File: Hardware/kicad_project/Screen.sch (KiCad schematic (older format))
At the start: 9 parts

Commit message: update project with corrected schematic / pcb
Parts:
- C51, C52, C53, C54: renamed from C?; footprint RandomJunk:C_0603_nosilk -> Capacitors_SMD:C_0402_NoSilk; LCSC c19702 -> C52923
- C55, C56: renamed from C?; footprint RandomJunk:C_0603_nosilk -> Capacitors_SMD:C_0402_NoSilk; LCSC c19702 -> C15525
- LCD1: renamed from LCD?; footprint (none) -> RandomJunk:oled_ssd1306_14pin_91
- R14: renamed from R?; footprint (none) -> Resistors_SMD:R_0402_NoSilk; LCSC (none) -> C25744
- R15: renamed from R?; footprint (none) -> Resistors_SMD:R_0402_NoSilk; LCSC (none) -> C25778
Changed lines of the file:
@@
 sda
 $Comp
-L customLibrary:128x32OLED LCD?
+L customLibrary:128x32OLED LCD1
 U 1 1 6364F37E
 P 6500 3750
-F 0 "LCD?" H 6828 3796 50  0000 L CNN
+F 0 "LCD1" H 6828 3796 50  0000 L CNN
 F 1 "128x32OLED" H 6828 3705 50  0000 L CNN
-F 2 "" H 6550 3800 50  0001 C CNN
+F 2 "RandomJunk:oled_ssd1306_14pin_91" H 6550 3800 50  0001 C CNN
 F 3 "" H 6550 3800 50  0001 C CNN
 	1    6500 3750
@@
 $EndComp
 $Comp
-L Device:C C?
+L Device:C C51
 U 1 1 6364F385
 P 5750 3100
-F 0 "C?" H 5865 3146 50  0000 L CNN
+F 0 "C51" H 5865 3146 50  0000 L CNN
 F 1 "1u" H 5865 3055 50  0000 L CNN
-F 2 "RandomJunk:C_0603_nosilk" H 5788 2950 50  0001 C CNN
-F 3 "~" H 5750 3100 50  0001 C CNN
-F 4 "c19702" H 5750 3100 50  0001 C CNN "LCSC"
+F 2 "Capacitors_SMD:C_0402_NoSilk" H 5788 2950 50  0001 C CNN
+F 3 "" H 5750 3100 50  0001 C CNN
+F 4 "C52923" H 5750 3100 50  0001 C CNN "LCSC"
 	1    5750 3100
 	0    1    1    0
 $EndComp
 $Comp
-L Device:C C?
+L Device:C C52
 U 1 1 6364F38C
 P 5450 3300
-F 0 "C?" H 5565 3346 50  0000 L CNN
+F 0 "C52" H 5565 3346 50  0000 L CNN
 F 1 "1u" H 5565 3255 50  0000 L CNN
-F 2 "RandomJunk:C_0603_nosilk" H 5488 3150 50  0001 C CNN
+F 2 "Capacitors_SMD:C_0402_NoSilk" H 5488 3150 50  0001 C CNN
 F 3 "~" H 5450 3300 50  0001 C CNN
-F 4 "c19702" H 5450 3300 50  0001 C CNN "LCSC"
+F 4 "C52923" H 5450 3300 50  0001 C CNN "LCSC"
 	1    5450 3300
 	0    1    1    0
@@
 	5200 3400 6100 3400
 $Comp
-L Device:C C?
+L Device:C C53
 U 1 1 6364F39B
 P 4700 3500
-F 0 "C?" H 4815 3546 50  0000 L CNN
+F 0 "C53" H 4815 3546 50  0000 L CNN
 F 1 "1u" H 4815 3455 50  0000 L CNN
-F 2 "RandomJunk:C_0603_nosilk" H 4738 3350 50  0001 C CNN
+F 2 "Capacitors_SMD:C_0402_NoSilk" H 4738 3350 50  0001 C CNN
 F 3 "~" H 4700 3500 50  0001 C CNN
-F 4 "c19702" H 4700 3500 50  0001 C CNN "LCSC"
+F 4 "C52923" H 4700 3500 50  0001 C CNN "LCSC"
 	1    4700 3500
 	0    1    1    0
 $EndComp
 $Comp
-L Device:C C?
+L Device:C C54
 U 1 1 6364F3A2
 P 4700 3800
-F 0 "C?" H 4815 3846 50  0000 L CNN
+F 0 "C54" H 4815 3846 50  0000 L CNN
 F 1 "1u" H 4815 3755 50  0000 L CNN
-F 2 "RandomJunk:C_0603_nosilk" H 4738 3650 50  0001 C CNN
+F 2 "Capacitors_SMD:C_0402_NoSilk" H 4738 3650 50  0001 C CNN
 F 3 "~" H 4700 3800 50  0001 C CNN
-F 4 "c19702" H 4700 3800 50  0001 C CNN "LCSC"
+F 4 "C52923" H 4700 3800 50  0001 C CNN "LCSC"
 	1    4700 3800
 	0    1    1    0
 $EndComp
 $Comp
-L power:+3.3V #PWR?
+L power:+3.3V #PWR039
 U 1 1 6364F3A8
 P 4900 3300
-F 0 "#PWR?" H 4900 3150 50  0001 C CNN
+F 0 "#PWR039" H 4900 3150 50  0001 C CNN
 F 1 "+3.3V" H 4915 3473 50  0000 C CNN
 F 2 "" H 4900 3300 50  0001 C CNN
@@
 $EndComp
 $Comp
-L power:+3.3V #PWR?
+L power:+3.3V #PWR038
 U 1 1 6364F3AE
 P 5100 3100
-F 0 "#PWR?" H 5100 2950 50  0001 C CNN
+F 0 "#PWR038" H 5100 2950 50  0001 C CNN
 F 1 "+3.3V" H 5115 3273 50  0000 C CNN
 F 2 "" H 5100 3100 50  0001 C CNN
@@
 	5100 3800 6100 3800
 $Comp
-L power:GND #PWR?
+L power:GND #PWR040
 U 1 1 6364F3BB
 P 4450 4600
-F 0 "#PWR?" H 4450 4350 50  0001 C CNN
+F 0 "#PWR040" H 4450 4350 50  0001 C CNN
 F 1 "GND" V 4455 4472 50  0000 R CNN
 F 2 "" H 4450 4600 50  0001 C CNN
@@
 $EndComp
 $Comp
-L Device:C C?
+L Device:C C56
 U 1 1 6364F3C2
 P 4950 4400
-F 0 "C?" H 5065 4446 50  0000 L CNN
+F 0 "C56" H 5065 4446 50  0000 L CNN
 F 1 "10u" H 5065 4355 50  0000 L CNN
-F 2 "RandomJunk:C_0603_nosilk" H 4988 4250 50  0001 C CNN
+F 2 "Capacitors_SMD:C_0402_NoSilk" H 4988 4250 50  0001 C CNN
 F 3 "~" H 4950 4400 50  0001 C CNN
-F 4 "c19702" H 4950 4400 50  0001 C CNN "LCSC"
+F 4 "C15525" H 4950 4400 50  0001 C CNN "LCSC"
 	1    4950 4400
 	0    1    1    0
 $EndComp
 $Comp
-L Device:C C?
+L Device:C C55
 U 1 1 6364F3C9
 P 5400 4300
-F 0 "C?" H 5515 4346 50  0000 L CNN
+F 0 "C55" H 5515 4346 50  0000 L CNN
 F 1 "10u" H 5515 4255 50  0000 L CNN
-F 2 "RandomJunk:C_0603_nosilk" H 5438 4150 50  0001 C CNN
+F 2 "Capacitors_SMD:C_0402_NoSilk" H 5438 4150 50  0001 C CNN
 F 3 "~" H 5400 4300 50  0001 C CNN
-F 4 "c19702" H 5400 4300 50  0001 C CNN "LCSC"
+F 4 "C15525" H 5400 4300 50  0001 C CNN "LCSC"
 	1    5400 4300
 	0    1    1    0
 $EndComp
 $Comp
-L Device:R R?
+L Device:R R15
 U 1 1 6364F3CF
 P 5750 4200
-F 0 "R?" V 5543 4200 50  0000 C CNN
+F 0 "R15" V 5543 4200 50  0000 C CNN
 F 1 "330k" V 5634 4200 50  0000 C CNN
-F 2 "" V 5680 4200 50  0001 C CNN
+F 2 "Resistors_SMD:R_0402_NoSilk" V 5680 4200 50  0001 C CNN
 F 3 "~" H 5750 4200 50  0001 C CNN
+F 4 "C25778" H 5750 4200 50  0001 C CNN "LCSC"
 	1    5750 4200
 	0    1    1    0
@@
 	4450 3700 4450 3800
 $Comp
-L Device:R R?
+L Device:R R14
 U 1 1 6364F3E9
 P 5450 3900
-F 0 "R?" V 5243 3900 50  0000 C CNN
+F 0 "R14" V 5243 3900 50  0000 C CNN
 F 1 "10k" V 5334 3900 50  0000 C CNN
-F 2 "" V 5380 3900 50  0001 C CNN
+F 2 "Resistors_SMD:R_0402_NoSilk" V 5380 3900 50  0001 C CNN
 F 3 "~" H 5450 3900 50  0001 C CNN
+F 4 "C25744" H 5450 3900 50  0001 C CNN "LCSC"
 	1    5450 3900
 	0    1    1    0

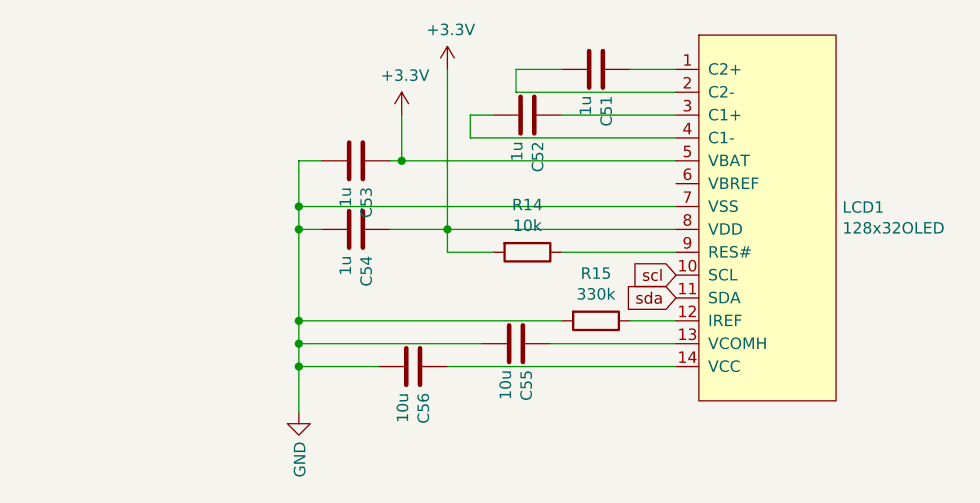
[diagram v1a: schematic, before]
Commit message: new hardware rev
- soft / latching power switch
- corrected mic
- added pullup to flash ss
- front & back enclosure plates
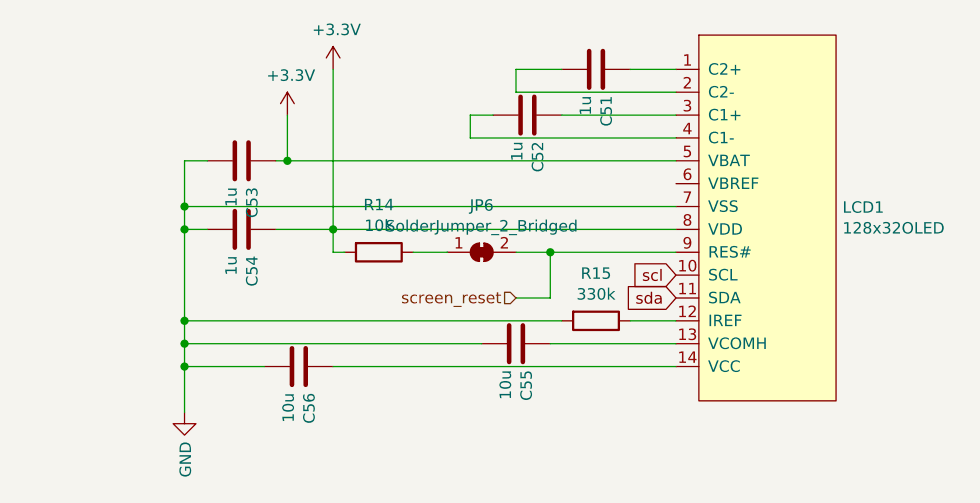
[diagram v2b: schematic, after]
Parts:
- added JP6: SolderJumper_2_Bridged, Jumper:SolderJumper-2_P1.3mm_Bridged_RoundedPad1.0x1.5mm, symbol Jumper:SolderJumper_2_Bridged
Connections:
- net at R14.1: now also JP6.1 (A); no longer LCD1.9 (RES#)
- new net screen_reset: JP6.2 (B), LCD1.9 (RES#)
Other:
- moved on the sheet: C53, C54, C56, R14
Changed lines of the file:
@@
 L Device:C C53
 U 1 1 6364F39B
-P 4700 3500
-F 0 "C53" H 4815 3546 50  0000 L CNN
-F 1 "1u" H 4815 3455 50  0000 L CNN
-F 2 "Capacitors_SMD:C_0402_NoSilk" H 4738 3350 50  0001 C CNN
-F 3 "~" H 4700 3500 50  0001 C CNN
-F 4 "C52923" H 4700 3500 50  0001 C CNN "LCSC"
-	1    4700 3500
+P 4200 3500
+F 0 "C53" H 4315 3546 50  0000 L CNN
+F 1 "1u" H 4315 3455 50  0000 L CNN
+F 2 "Capacitors_SMD:C_0402_NoSilk" H 4238 3350 50  0001 C CNN
+F 3 "~" H 4200 3500 50  0001 C CNN
+F 4 "C52923" H 4200 3500 50  0001 C CNN "LCSC"
+	1    4200 3500
 	0    1    1    0
 $EndComp
@@
 L Device:C C54
 U 1 1 6364F3A2
-P 4700 3800
-F 0 "C54" H 4815 3846 50  0000 L CNN
-F 1 "1u" H 4815 3755 50  0000 L CNN
-F 2 "Capacitors_SMD:C_0402_NoSilk" H 4738 3650 50  0001 C CNN
-F 3 "~" H 4700 3800 50  0001 C CNN
-F 4 "C52923" H 4700 3800 50  0001 C CNN "LCSC"
-	1    4700 3800
+P 4200 3800
+F 0 "C54" H 4315 3846 50  0000 L CNN
+F 1 "1u" H 4315 3755 50  0000 L CNN
+F 2 "Capacitors_SMD:C_0402_NoSilk" H 4238 3650 50  0001 C CNN
+F 3 "~" H 4200 3800 50  0001 C CNN
+F 4 "C52923" H 4200 3800 50  0001 C CNN "LCSC"
+	1    4200 3800
 	0    1    1    0
 $EndComp
@@
 L power:+3.3V #PWR039
 U 1 1 6364F3A8
-P 4900 3300
-F 0 "#PWR039" H 4900 3150 50  0001 C CNN
-F 1 "+3.3V" H 4915 3473 50  0000 C CNN
-F 2 "" H 4900 3300 50  0001 C CNN
-F 3 "" H 4900 3300 50  0001 C CNN
-	1    4900 3300
+P 4400 3300
+F 0 "#PWR039" H 4400 3150 50  0001 C CNN
+F 1 "+3.3V" H 4415 3473 50  0000 C CNN
+F 2 "" H 4400 3300 50  0001 C CNN
+F 3 "" H 4400 3300 50  0001 C CNN
+	1    4400 3300
 	1    0    0    -1
 $EndComp
@@
 L power:+3.3V #PWR038
 U 1 1 6364F3AE
-P 5100 3100
-F 0 "#PWR038" H 5100 2950 50  0001 C CNN
-F 1 "+3.3V" H 5115 3273 50  0000 C CNN
-F 2 "" H 5100 3100 50  0001 C CNN
-F 3 "" H 5100 3100 50  0001 C CNN
-	1    5100 3100
+P 4600 3100
+F 0 "#PWR038" H 4600 2950 50  0001 C CNN
+F 1 "+3.3V" H 4615 3273 50  0000 C CNN
+F 2 "" H 4600 3100 50  0001 C CNN
+F 3 "" H 4600 3100 50  0001 C CNN
+	1    4600 3100
 	1    0    0    -1
 $EndComp
 Wire Wire Line
-	6100 3500 4900 3500
+	6100 3500 4400 3500
 Wire Wire Line
-	4900 3300 4900 3500
-Connection ~ 4900 3500
+	4400 3300 4400 3500
+Connection ~ 4400 3500
 Wire Wire Line
-	4900 3500 4850 3500
+	4400 3500 4350 3500
 Wire Wire Line
-	4850 3800 5100 3800
-Connection ~ 5100 3800
+	4350 3800 4600 3800
+Connection ~ 4600 3800
 Wire Wire Line
-	5100 3800 6100 3800
+	4600 3800 6100 3800
 $Comp
 L power:GND #PWR040
 U 1 1 6364F3BB
-P 4450 4600
-F 0 "#PWR040" H 4450 4350 50  0001 C CNN
-F 1 "GND" V 4455 4472 50  0000 R CNN
-F 2 "" H 4450 4600 50  0001 C CNN
-F 3 "" H 4450 4600 50  0001 C CNN
-	1    4450 4600
+P 3950 4600
+F 0 "#PWR040" H 3950 4350 50  0001 C CNN
+F 1 "GND" V 3955 4472 50  0000 R CNN
+F 2 "" H 3950 4600 50  0001 C CNN
+F 3 "" H 3950 4600 50  0001 C CNN
+	1    3950 4600
 	1    0    0    -1
 $EndComp
@@
 L Device:C C56
 U 1 1 6364F3C2
-P 4950 4400
-F 0 "C56" H 5065 4446 50  0000 L CNN
-F 1 "10u" H 5065 4355 50  0000 L CNN
-F 2 "Capacitors_SMD:C_0402_NoSilk" H 4988 4250 50  0001 C CNN
-F 3 "~" H 4950 4400 50  0001 C CNN
-F 4 "C15525" H 4950 4400 50  0001 C CNN "LCSC"
-	1    4950 4400
+P 4450 4400
+F 0 "C56" H 4565 4446 50  0000 L CNN
+F 1 "10u" H 4565 4355 50  0000 L CNN
+F 2 "Capacitors_SMD:C_0402_NoSilk" H 4488 4250 50  0001 C CNN
+F 3 "~" H 4450 4400 50  0001 C CNN
+F 4 "C15525" H 4450 4400 50  0001 C CNN "LCSC"
+	1    4450 4400
 	0    1    1    0
 $EndComp
@@
 	6100 4200 5900 4200
 Wire Wire Line
-	5600 4200 4450 4200
+	5600 4200 3950 4200
 Wire Wire Line
-	4450 4200 4450 4300
+	3950 4200 3950 4300
 Wire Wire Line
 	6100 4300 5550 4300
 Wire Wire Line
-	5250 4300 4450 4300
-Connection ~ 4450 4300
+	5250 4300 3950 4300
+Connection ~ 3950 4300
 Wire Wire Line
-	4450 4300 4450 4400
+	3950 4300 3950 4400
 Wire Wire Line
-	4800 4400 4450 4400
-Connection ~ 4450 4400
+	4300 4400 3950 4400
+Connection ~ 3950 4400
 Wire Wire Line
-	4450 4400 4450 4600
+	3950 4400 3950 4600
 Wire Wire Line
-	5100 4400 6100 4400
+	4600 4400 6100 4400
 Wire Wire Line
-	4550 3800 4450 3800
-Connection ~ 4450 4200
+	4050 3800 3950 3800
+Connection ~ 3950 4200
 Wire Wire Line
-	4550 3500 4450 3500
+	4050 3500 3950 3500
 Wire Wire Line
-	4450 3500 4450 3700
-Connection ~ 4450 3800
+	3950 3500 3950 3700
+Connection ~ 3950 3800
 Wire Wire Line
-	4450 3800 4450 4200
+	3950 3800 3950 4200
 Wire Wire Line
-	4450 3700 6100 3700
-Connection ~ 4450 3700
+	3950 3700 6100 3700
+Connection ~ 3950 3700
 Wire Wire Line
-	4450 3700 4450 3800
+	3950 3700 3950 3800
 $Comp
 L Device:R R14
 U 1 1 6364F3E9
-P 5450 3900
-F 0 "R14" V 5243 3900 50  0000 C CNN
-F 1 "10k" V 5334 3900 50  0000 C CNN
-F 2 "Resistors_SMD:R_0402_NoSilk" V 5380 3900 50  0001 C CNN
-F 3 "~" H 5450 3900 50  0001 C CNN
-F 4 "C25744" H 5450 3900 50  0001 C CNN "LCSC"
-	1    5450 3900
+P 4800 3900
+F 0 "R14" V 4593 3900 50  0000 C CNN
+F 1 "10k" V 4684 3900 50  0000 C CNN
+F 2 "Resistors_SMD:R_0402_NoSilk" V 4730 3900 50  0001 C CNN
+F 3 "~" H 4800 3900 50  0001 C CNN
+F 4 "C25744" H 4800 3900 50  0001 C CNN "LCSC"
+	1    4800 3900
 	0    1    1    0
 $EndComp
 Wire Wire Line
-	6100 3900 5600 3900
+	6100 3900 5550 3900
 Wire Wire Line
-	5100 3100 5100 3800
+	4600 3100 4600 3800
 Wire Wire Line
-	5300 3900 5100 3900
+	4650 3900 4600 3900
 Wire Wire Line
-	5100 3900 5100 3800
+	4600 3900 4600 3800
+Text HLabel 5400 4100 0    50   Input ~ 0
+screen_reset
+$Comp
+L Jumper:SolderJumper_2_Bridged JP6
+U 1 1 61E0FF09
+P 5250 3900
+F 0 "JP6" H 5250 4105 50  0000 C CNN
+F 1 "SolderJumper_2_Bridged" H 5250 4014 50  0000 C CNN
+F 2 "Jumper:SolderJumper-2_P1.3mm_Bridged_RoundedPad1.0x1.5mm" H 5250 3900 50  0001 C CNN
+F 3 "~" H 5250 3900 50  0001 C CNN
+	1    5250 3900
+	1    0    0    -1
+$EndComp
+Wire Wire Line
+	5100 3900 4950 3900
+Wire Wire Line
+	5400 4100 5550 4100
+Wire Wire Line
+	5550 4100 5550 3900
+Connection ~ 5550 3900
+Wire Wire Line
+	5550 3900 5400 3900
 $EndSCHEMATC
